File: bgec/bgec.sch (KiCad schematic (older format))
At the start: 6 parts

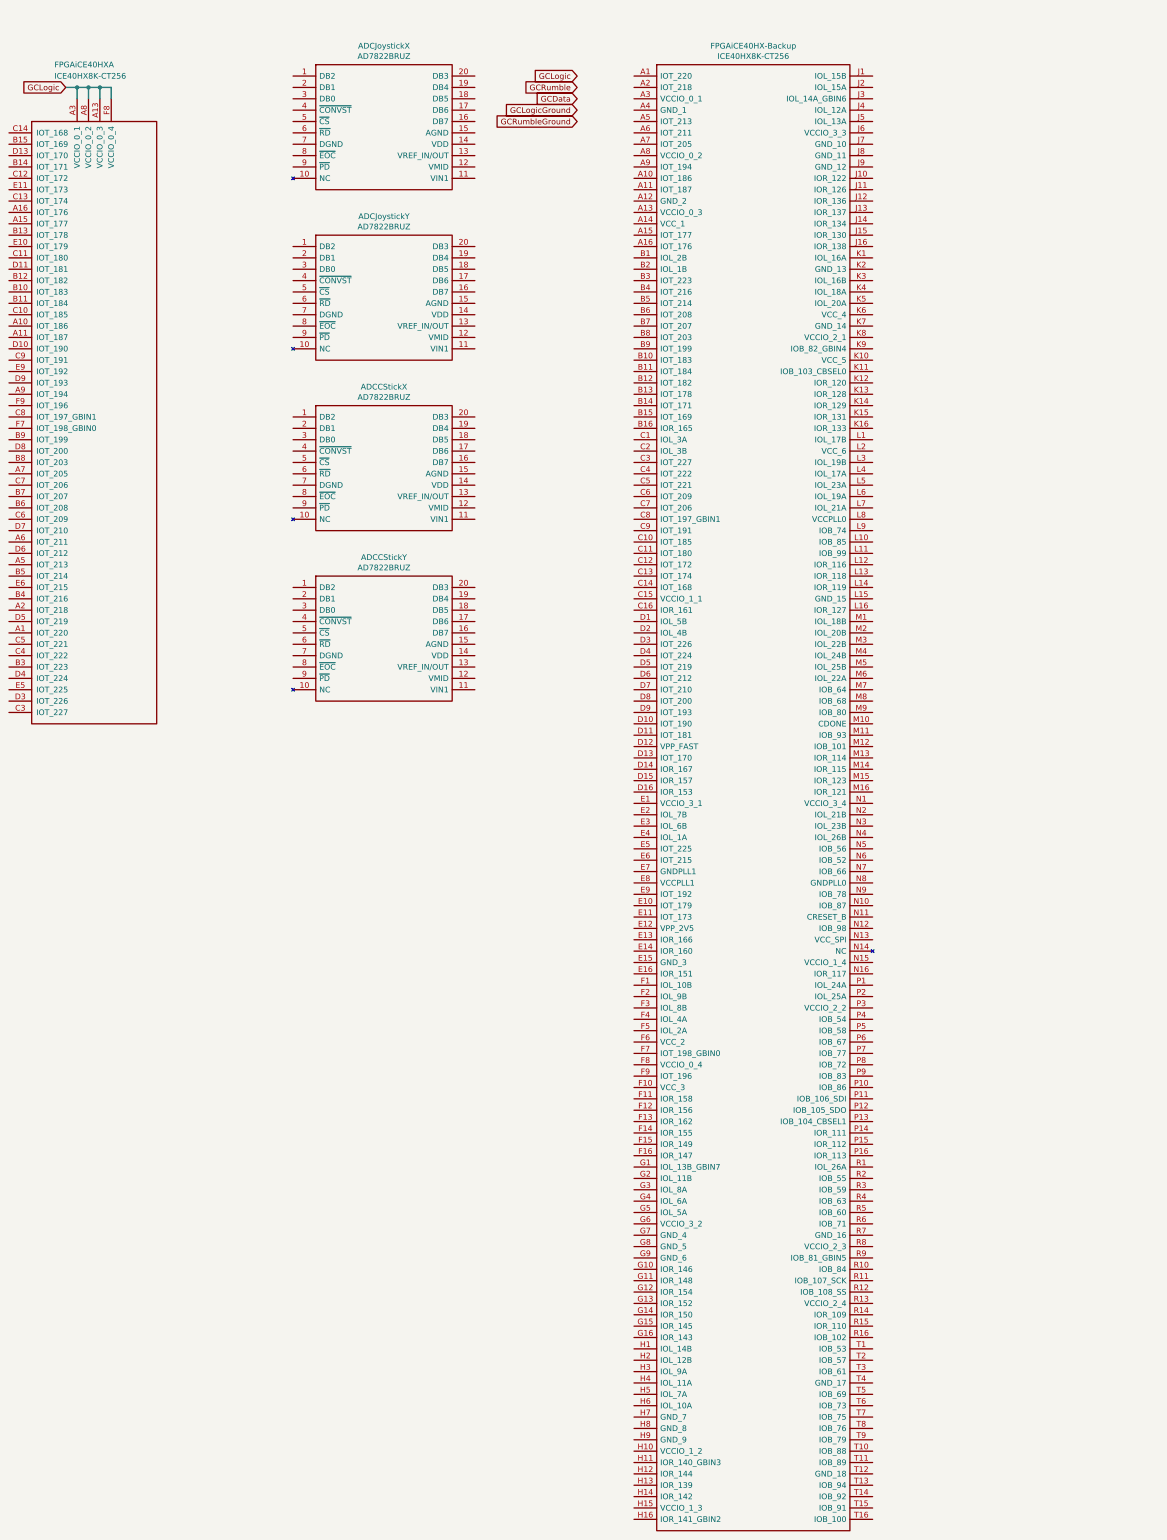
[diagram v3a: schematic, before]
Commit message: Add second IO bank to the FPGA schematic, move ADC to local library
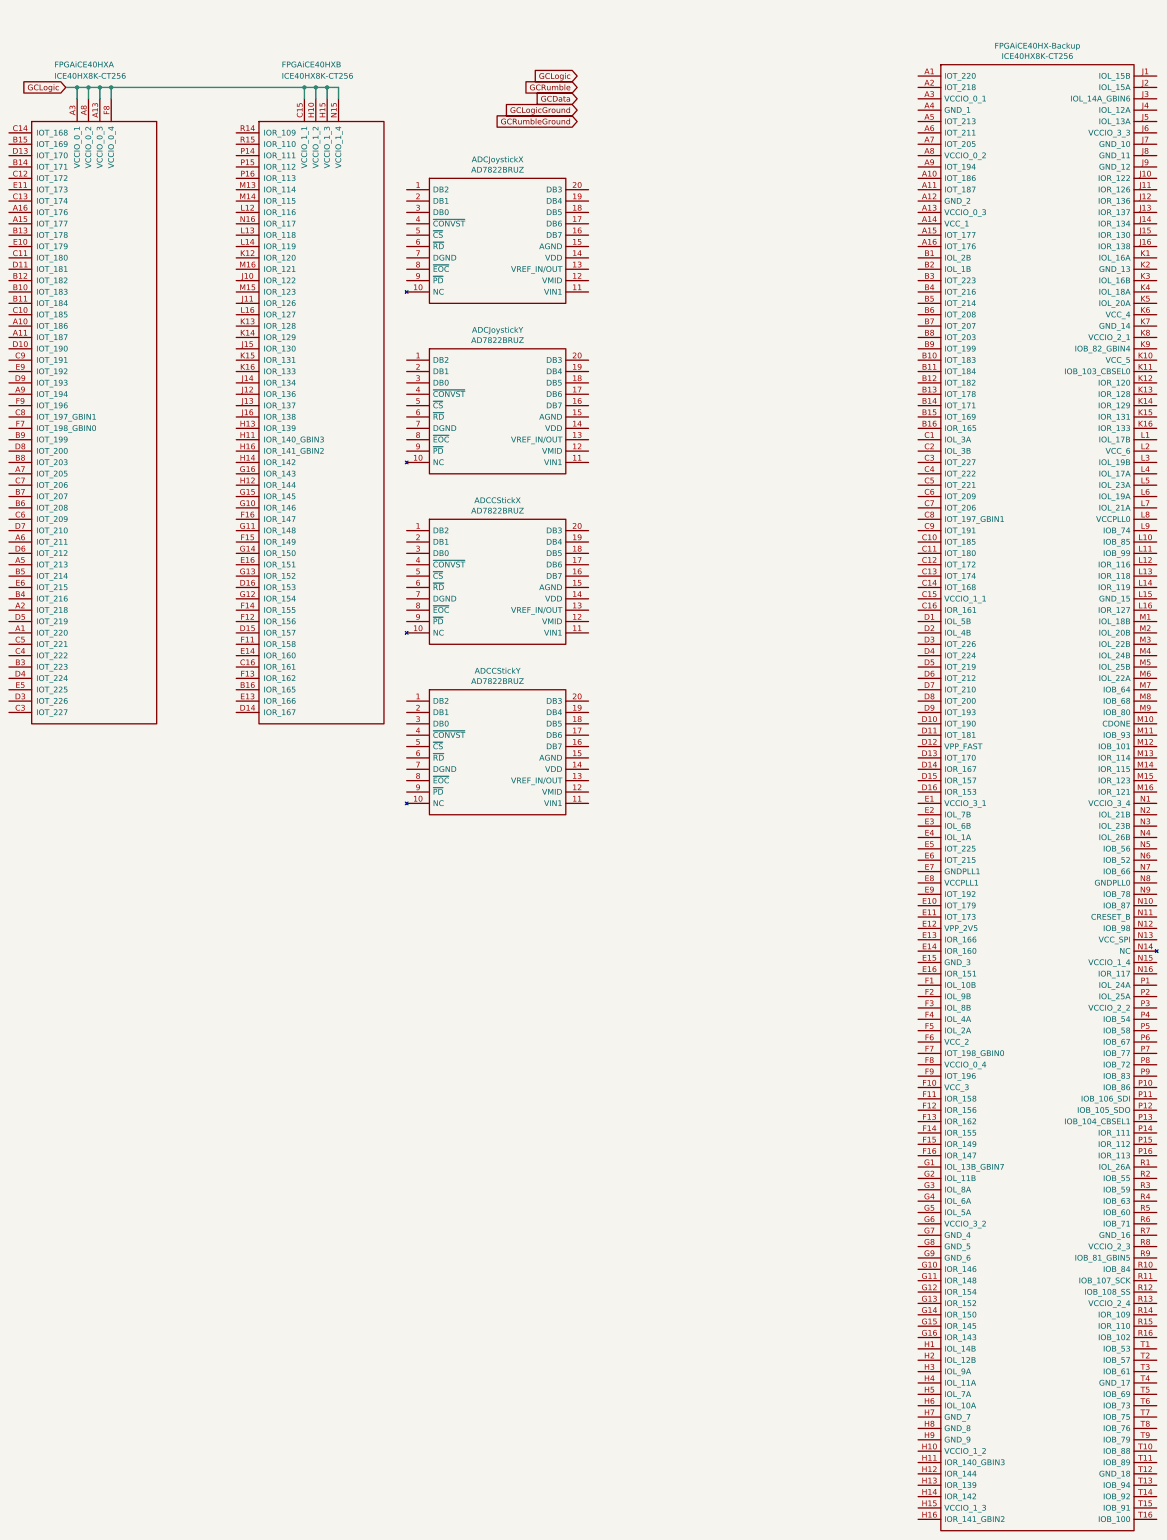
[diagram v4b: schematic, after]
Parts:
- added unit 2 of FPGAiCE40HX
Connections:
- net GCLogic: now also FPGAiCE40HX.C15 (VCCIO_1_1), FPGAiCE40HX.H10 (VCCIO_1_2), FPGAiCE40HX.H15 (VCCIO_1_3), FPGAiCE40HX.N15 (VCCIO_1_4)
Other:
- moved on the sheet: ADCCStickX, ADCCStickY, ADCJoystickX, ADCJoystickY, FPGAiCE40HX-Backup
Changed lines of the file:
@@
 L LibraryLoader:AD7822BRUZ ADCJoystickX
 U 1 1 5E4E3FD4
-P 3500 1000
-F 0 "ADCJoystickX" H 4300 1265 50  0000 C CNN
-F 1 "AD7822BRUZ" H 4300 1174 50  0000 C CNN
-F 2 "SOP65P640X120-20N" H 4950 1100 50  0001 L CNN
-F 3 "https://componentsearchengine.com/Datasheets/1/AD7822BRUZ.pdf" H 4950 1000 50  0001 L CNN
-F 4 "AD7822BRUZ, 8 bit ADC, Parallel, 20-Pin TSSOP" H 4950 900 50  0001 L CNN "Description"
-F 5 "1.2" H 4950 800 50  0001 L CNN "Height"
-F 6 "584-AD7822BRUZ" H 4950 700 50  0001 L CNN "Mouser Part Number"
-F 7 "https://www.mouser.com/Search/Refine.aspx?Keyword=584-AD7822BRUZ" H 4950 600 50  0001 L CNN "Mouser Price/Stock"
-F 8 "Analog Devices" H 4950 500 50  0001 L CNN "Manufacturer_Name"
-F 9 "AD7822BRUZ" H 4950 400 50  0001 L CNN "Manufacturer_Part_Number"
-	1    3500 1000
+P 4500 2000
+F 0 "ADCJoystickX" H 5300 2265 50  0000 C CNN
+F 1 "AD7822BRUZ" H 5300 2174 50  0000 C CNN
+F 2 "SOP65P640X120-20N" H 5950 2100 50  0001 L CNN
+F 3 "https://componentsearchengine.com/Datasheets/1/AD7822BRUZ.pdf" H 5950 2000 50  0001 L CNN
+F 4 "AD7822BRUZ, 8 bit ADC, Parallel, 20-Pin TSSOP" H 5950 1900 50  0001 L CNN "Description"
+F 5 "1.2" H 5950 1800 50  0001 L CNN "Height"
+F 6 "584-AD7822BRUZ" H 5950 1700 50  0001 L CNN "Mouser Part Number"
+F 7 "https://www.mouser.com/Search/Refine.aspx?Keyword=584-AD7822BRUZ" H 5950 1600 50  0001 L CNN "Mouser Price/Stock"
+F 8 "Analog Devices" H 5950 1500 50  0001 L CNN "Manufacturer_Name"
+F 9 "AD7822BRUZ" H 5950 1400 50  0001 L CNN "Manufacturer_Part_Number"
+	1    4500 2000
 	1    0    0    -1
 $EndComp
@@
 L LibraryLoader:AD7822BRUZ ADCJoystickY
 U 1 1 5E4E4DBF
-P 3500 2500
-F 0 "ADCJoystickY" H 4300 2765 50  0000 C CNN
-F 1 "AD7822BRUZ" H 4300 2674 50  0000 C CNN
-F 2 "SOP65P640X120-20N" H 4950 2600 50  0001 L CNN
-F 3 "https://componentsearchengine.com/Datasheets/1/AD7822BRUZ.pdf" H 4950 2500 50  0001 L CNN
-F 4 "AD7822BRUZ, 8 bit ADC, Parallel, 20-Pin TSSOP" H 4950 2400 50  0001 L CNN "Description"
-F 5 "1.2" H 4950 2300 50  0001 L CNN "Height"
-F 6 "584-AD7822BRUZ" H 4950 2200 50  0001 L CNN "Mouser Part Number"
-F 7 "https://www.mouser.com/Search/Refine.aspx?Keyword=584-AD7822BRUZ" H 4950 2100 50  0001 L CNN "Mouser Price/Stock"
-F 8 "Analog Devices" H 4950 2000 50  0001 L CNN "Manufacturer_Name"
-F 9 "AD7822BRUZ" H 4950 1900 50  0001 L CNN "Manufacturer_Part_Number"
-	1    3500 2500
+P 4500 3500
+F 0 "ADCJoystickY" H 5300 3765 50  0000 C CNN
+F 1 "AD7822BRUZ" H 5300 3674 50  0000 C CNN
+F 2 "SOP65P640X120-20N" H 5950 3600 50  0001 L CNN
+F 3 "https://componentsearchengine.com/Datasheets/1/AD7822BRUZ.pdf" H 5950 3500 50  0001 L CNN
+F 4 "AD7822BRUZ, 8 bit ADC, Parallel, 20-Pin TSSOP" H 5950 3400 50  0001 L CNN "Description"
+F 5 "1.2" H 5950 3300 50  0001 L CNN "Height"
+F 6 "584-AD7822BRUZ" H 5950 3200 50  0001 L CNN "Mouser Part Number"
+F 7 "https://www.mouser.com/Search/Refine.aspx?Keyword=584-AD7822BRUZ" H 5950 3100 50  0001 L CNN "Mouser Price/Stock"
+F 8 "Analog Devices" H 5950 3000 50  0001 L CNN "Manufacturer_Name"
+F 9 "AD7822BRUZ" H 5950 2900 50  0001 L CNN "Manufacturer_Part_Number"
+	1    4500 3500
 	1    0    0    -1
 $EndComp
@@
 L LibraryLoader:AD7822BRUZ ADCCStickX
 U 1 1 5E4E5FF1
-P 3500 4000
-F 0 "ADCCStickX" H 4300 4265 50  0000 C CNN
-F 1 "AD7822BRUZ" H 4300 4174 50  0000 C CNN
-F 2 "SOP65P640X120-20N" H 4950 4100 50  0001 L CNN
-F 3 "https://componentsearchengine.com/Datasheets/1/AD7822BRUZ.pdf" H 4950 4000 50  0001 L CNN
-F 4 "AD7822BRUZ, 8 bit ADC, Parallel, 20-Pin TSSOP" H 4950 3900 50  0001 L CNN "Description"
-F 5 "1.2" H 4950 3800 50  0001 L CNN "Height"
-F 6 "584-AD7822BRUZ" H 4950 3700 50  0001 L CNN "Mouser Part Number"
-F 7 "https://www.mouser.com/Search/Refine.aspx?Keyword=584-AD7822BRUZ" H 4950 3600 50  0001 L CNN "Mouser Price/Stock"
-F 8 "Analog Devices" H 4950 3500 50  0001 L CNN "Manufacturer_Name"
-F 9 "AD7822BRUZ" H 4950 3400 50  0001 L CNN "Manufacturer_Part_Number"
-	1    3500 4000
+P 4500 5000
+F 0 "ADCCStickX" H 5300 5265 50  0000 C CNN
+F 1 "AD7822BRUZ" H 5300 5174 50  0000 C CNN
+F 2 "SOP65P640X120-20N" H 5950 5100 50  0001 L CNN
+F 3 "https://componentsearchengine.com/Datasheets/1/AD7822BRUZ.pdf" H 5950 5000 50  0001 L CNN
+F 4 "AD7822BRUZ, 8 bit ADC, Parallel, 20-Pin TSSOP" H 5950 4900 50  0001 L CNN "Description"
+F 5 "1.2" H 5950 4800 50  0001 L CNN "Height"
+F 6 "584-AD7822BRUZ" H 5950 4700 50  0001 L CNN "Mouser Part Number"
+F 7 "https://www.mouser.com/Search/Refine.aspx?Keyword=584-AD7822BRUZ" H 5950 4600 50  0001 L CNN "Mouser Price/Stock"
+F 8 "Analog Devices" H 5950 4500 50  0001 L CNN "Manufacturer_Name"
+F 9 "AD7822BRUZ" H 5950 4400 50  0001 L CNN "Manufacturer_Part_Number"
+	1    4500 5000
 	1    0    0    -1
 $EndComp
@@
 L LibraryLoader:AD7822BRUZ ADCCStickY
 U 1 1 5E4E6A54
-P 3500 5500
-F 0 "ADCCStickY" H 4300 5765 50  0000 C CNN
-F 1 "AD7822BRUZ" H 4300 5674 50  0000 C CNN
-F 2 "SOP65P640X120-20N" H 4950 5600 50  0001 L CNN
-F 3 "https://componentsearchengine.com/Datasheets/1/AD7822BRUZ.pdf" H 4950 5500 50  0001 L CNN
-F 4 "AD7822BRUZ, 8 bit ADC, Parallel, 20-Pin TSSOP" H 4950 5400 50  0001 L CNN "Description"
-F 5 "1.2" H 4950 5300 50  0001 L CNN "Height"
-F 6 "584-AD7822BRUZ" H 4950 5200 50  0001 L CNN "Mouser Part Number"
-F 7 "https://www.mouser.com/Search/Refine.aspx?Keyword=584-AD7822BRUZ" H 4950 5100 50  0001 L CNN "Mouser Price/Stock"
-F 8 "Analog Devices" H 4950 5000 50  0001 L CNN "Manufacturer_Name"
-F 9 "AD7822BRUZ" H 4950 4900 50  0001 L CNN "Manufacturer_Part_Number"
-	1    3500 5500
+P 4500 6500
+F 0 "ADCCStickY" H 5300 6765 50  0000 C CNN
+F 1 "AD7822BRUZ" H 5300 6674 50  0000 C CNN
+F 2 "SOP65P640X120-20N" H 5950 6600 50  0001 L CNN
+F 3 "https://componentsearchengine.com/Datasheets/1/AD7822BRUZ.pdf" H 5950 6500 50  0001 L CNN
+F 4 "AD7822BRUZ, 8 bit ADC, Parallel, 20-Pin TSSOP" H 5950 6400 50  0001 L CNN "Description"
+F 5 "1.2" H 5950 6300 50  0001 L CNN "Height"
+F 6 "584-AD7822BRUZ" H 5950 6200 50  0001 L CNN "Mouser Part Number"
+F 7 "https://www.mouser.com/Search/Refine.aspx?Keyword=584-AD7822BRUZ" H 5950 6100 50  0001 L CNN "Mouser Price/Stock"
+F 8 "Analog Devices" H 5950 6000 50  0001 L CNN "Manufacturer_Name"
+F 9 "AD7822BRUZ" H 5950 5900 50  0001 L CNN "Manufacturer_Part_Number"
+	1    4500 6500
 	1    0    0    -1
 $EndComp
@@
 L LibraryLoader:ICE40HX8K-CT256 FPGAiCE40HX-Backup
 U 1 1 5E4F6C64
-P 6500 1000
-F 0 "FPGAiCE40HX-Backup" H 7550 1265 50  0000 C CNN
-F 1 "ICE40HX8K-CT256" H 7550 1174 50  0000 C CNN
-F 2 "BGA256C80P16X16_1400X1400X170" H 8450 1100 50  0001 L CNN
-F 3 "https://componentsearchengine.com/Datasheets/1/iCE40HX8K-CT256.pdf" H 8450 1000 50  0001 L CNN
-F 4 "FPGA iCE40 HX Family 7680 Cells 40nm Technology 1.2V 256-Pin CSBGA" H 8450 900 50  0001 L CNN "Description"
-F 5 "1.7" H 8450 800 50  0001 L CNN "Height"
-F 6 "842-ICE40HX8K-CT256" H 8450 700 50  0001 L CNN "Mouser Part Number"
-F 7 "https://www.mouser.com/Search/Refine.aspx?Keyword=842-ICE40HX8K-CT256" H 8450 600 50  0001 L CNN "Mouser Price/Stock"
-F 8 "Lattice Semiconductor" H 8450 500 50  0001 L CNN "Manufacturer_Name"
-F 9 "ICE40HX8K-CT256" H 8450 400 50  0001 L CNN "Manufacturer_Part_Number"
-	1    6500 1000
+P 9000 1000
+F 0 "FPGAiCE40HX-Backup" H 10050 1265 50  0000 C CNN
+F 1 "ICE40HX8K-CT256" H 10050 1174 50  0000 C CNN
+F 2 "BGA256C80P16X16_1400X1400X170" H 10950 1100 50  0001 L CNN
+F 3 "https://componentsearchengine.com/Datasheets/1/iCE40HX8K-CT256.pdf" H 10950 1000 50  0001 L CNN
+F 4 "FPGA iCE40 HX Family 7680 Cells 40nm Technology 1.2V 256-Pin CSBGA" H 10950 900 50  0001 L CNN "Description"
+F 5 "1.7" H 10950 800 50  0001 L CNN "Height"
+F 6 "842-ICE40HX8K-CT256" H 10950 700 50  0001 L CNN "Mouser Part Number"
+F 7 "https://www.mouser.com/Search/Refine.aspx?Keyword=842-ICE40HX8K-CT256" H 10950 600 50  0001 L CNN "Mouser Price/Stock"
+F 8 "Lattice Semiconductor" H 10950 500 50  0001 L CNN "Manufacturer_Name"
+F 9 "ICE40HX8K-CT256" H 10950 400 50  0001 L CNN "Manufacturer_Part_Number"
+	1    9000 1000
 	1    0    0    -1
 $EndComp
@@
 	1900 1100 1900 1200
 Connection ~ 1800 1100
+$Comp
+L bgec-components:ICE40HX8K-CT256 FPGAiCE40HX
+U 2 1 5E506C35
+P 3000 1500
+F 0 "FPGAiCE40HX" H 3400 2100 50  0000 L CNN
+F 1 "ICE40HX8K-CT256" H 3400 2000 50  0000 L CNN
+F 2 "LibraryLoader:BGA256C80P16X16_1400X1400X170" H 4250 2500 50  0001 C CNN
+F 3 "http://www.latticesemi.com/Products/FPGAandCPLD/iCE40" H 4100 2400 50  0001 C CNN
+	2    3000 1500
+	1    0    0    -1
+$EndComp
+Wire Wire Line
+	1900 1100 3600 1100
+Wire Wire Line
+	3600 1100 3600 1200
+Connection ~ 1900 1100
+Wire Wire Line
+	3600 1100 3700 1100
+Wire Wire Line
+	3700 1100 3700 1200
+Connection ~ 3600 1100
+Wire Wire Line
+	3700 1100 3800 1100
+Wire Wire Line
+	3800 1100 3800 1200
+Connection ~ 3700 1100
+Wire Wire Line
+	3800 1100 3900 1100
+Wire Wire Line
+	3900 1100 3900 1200
+Connection ~ 3800 1100
 $EndSCHEMATC

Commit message: Get rid of external references
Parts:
- removed FPGAiCE40HX-Backup: ICE40HX8K-CT256, BGA256C80P16X16_1400X1400X170, symbol LibraryLoader:ICE40HX8K-CT256
- ADCCStickX, ADCCStickY, ADCJoystickX, ADCJoystickY: symbol LibraryLoader:AD7822BRUZ -> bgec-components:AD7822BRUZ
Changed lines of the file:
@@
 $EndDescr
 $Comp
-L LibraryLoader:AD7822BRUZ ADCJoystickX
+L bgec-components:AD7822BRUZ ADCJoystickX
 U 1 1 5E4E3FD4
 P 4500 2000
@@
 $EndComp
 $Comp
-L LibraryLoader:AD7822BRUZ ADCJoystickY
+L bgec-components:AD7822BRUZ ADCJoystickY
 U 1 1 5E4E4DBF
 P 4500 3500
@@
 $EndComp
 $Comp
-L LibraryLoader:AD7822BRUZ ADCCStickX
+L bgec-components:AD7822BRUZ ADCCStickX
 U 1 1 5E4E5FF1
 P 4500 5000
@@
 $EndComp
 $Comp
-L LibraryLoader:AD7822BRUZ ADCCStickY
+L bgec-components:AD7822BRUZ ADCCStickY
 U 1 1 5E4E6A54
 P 4500 6500
@@
 GCRumbleGround
 $Comp
-L LibraryLoader:ICE40HX8K-CT256 FPGAiCE40HX-Backup
-U 1 1 5E4F6C64
-P 9000 1000
-F 0 "FPGAiCE40HX-Backup" H 10050 1265 50  0000 C CNN
-F 1 "ICE40HX8K-CT256" H 10050 1174 50  0000 C CNN
-F 2 "BGA256C80P16X16_1400X1400X170" H 10950 1100 50  0001 L CNN
-F 3 "https://componentsearchengine.com/Datasheets/1/iCE40HX8K-CT256.pdf" H 10950 1000 50  0001 L CNN
-F 4 "FPGA iCE40 HX Family 7680 Cells 40nm Technology 1.2V 256-Pin CSBGA" H 10950 900 50  0001 L CNN "Description"
-F 5 "1.7" H 10950 800 50  0001 L CNN "Height"
-F 6 "842-ICE40HX8K-CT256" H 10950 700 50  0001 L CNN "Mouser Part Number"
-F 7 "https://www.mouser.com/Search/Refine.aspx?Keyword=842-ICE40HX8K-CT256" H 10950 600 50  0001 L CNN "Mouser Price/Stock"
-F 8 "Lattice Semiconductor" H 10950 500 50  0001 L CNN "Manufacturer_Name"
-F 9 "ICE40HX8K-CT256" H 10950 400 50  0001 L CNN "Manufacturer_Part_Number"
-	1    9000 1000
-	1    0    0    -1
-$EndComp
-$Comp
 L bgec-components:ICE40HX8K-CT256 FPGAiCE40HX

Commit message: Standardize library name and move footprints to local library
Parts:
- ADCCStickX, ADCCStickY, ADCJoystickX, ADCJoystickY: symbol bgec-components:AD7822BRUZ -> bgec:AD7822BRUZ
- FPGAiCE40HX: footprint LibraryLoader:BGA256C80P16X16_1400X1400X170 -> bgec:BGA256C80P16X16_1400X1400X170; symbol bgec-components:ICE40HX8K-CT256 -> bgec:ICE40HX8K-CT256
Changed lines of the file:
@@
 $EndDescr
 $Comp
-L bgec-components:AD7822BRUZ ADCJoystickX
+L bgec:AD7822BRUZ ADCJoystickX
 U 1 1 5E4E3FD4
 P 4500 2000
@@
 $EndComp
 $Comp
-L bgec-components:AD7822BRUZ ADCJoystickY
+L bgec:AD7822BRUZ ADCJoystickY
 U 1 1 5E4E4DBF
 P 4500 3500
@@
 $EndComp
 $Comp
-L bgec-components:AD7822BRUZ ADCCStickX
+L bgec:AD7822BRUZ ADCCStickX
 U 1 1 5E4E5FF1
 P 4500 5000
@@
 $EndComp
 $Comp
-L bgec-components:AD7822BRUZ ADCCStickY
+L bgec:AD7822BRUZ ADCCStickY
 U 1 1 5E4E6A54
 P 4500 6500
@@
 GCRumbleGround
 $Comp
-L bgec-components:ICE40HX8K-CT256 FPGAiCE40HX
+L bgec:ICE40HX8K-CT256 FPGAiCE40HX
 U 1 1 5E50B913
 P 1000 1500
 F 0 "FPGAiCE40HX" H 1400 2100 50  0000 L CNN
 F 1 "ICE40HX8K-CT256" H 1400 2000 50  0000 L CNN
-F 2 "LibraryLoader:BGA256C80P16X16_1400X1400X170" H 1750 2250 50  0001 C CNN
+F 2 "bgec:BGA256C80P16X16_1400X1400X170" H 1750 2250 50  0001 C CNN
 F 3 "http://www.latticesemi.com/Products/FPGAandCPLD/iCE40" H 1750 2250 50  0001 C CNN
 	1    1000 1500
@@
 Connection ~ 1800 1100
 $Comp
-L bgec-components:ICE40HX8K-CT256 FPGAiCE40HX
+L bgec:ICE40HX8K-CT256 FPGAiCE40HX
 U 2 1 5E506C35
 P 3000 1500
 F 0 "FPGAiCE40HX" H 3400 2100 50  0000 L CNN
 F 1 "ICE40HX8K-CT256" H 3400 2000 50  0000 L CNN
-F 2 "LibraryLoader:BGA256C80P16X16_1400X1400X170" H 4250 2500 50  0001 C CNN
+F 2 "bgec:BGA256C80P16X16_1400X1400X170" H 4250 2500 50  0001 C CNN
 F 3 "http://www.latticesemi.com/Products/FPGAandCPLD/iCE40" H 4100 2400 50  0001 C CNN
 	2    3000 1500
